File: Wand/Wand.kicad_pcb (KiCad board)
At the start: 4 copper layers, 50 x 7 mm, 20 parts, among them P1 ISP, P2 KLB4, P3 BASE, U1 ATMEGA328-MMH, U2 MAX31855KASA+, U3 MPU-6050

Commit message: Tidy up of the silk screen
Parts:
- moved C5 0.10 mm to (116.6, 112.7)

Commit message: Added back silk screen info
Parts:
- added G***: LOGO, Wand:RLAB_LOGO, B.Cu at (107.7, 112.0)
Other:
- board text added: "Hotstick - Wand"
- board text added: "Reading Hackspace - http://rlab.org.uk/"
- board text added: "rev 1 - 24/01/2016"

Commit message: Some more tidy ups
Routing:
- net /SCK: track 48.8 -> 47.4 mm
- net Net-(D1-Pad2): track 3.68 -> 4.59 mm

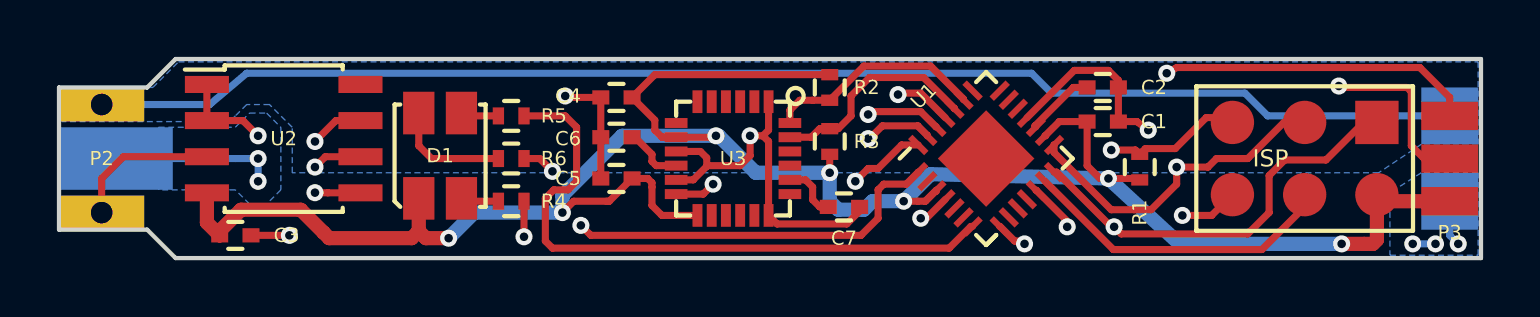
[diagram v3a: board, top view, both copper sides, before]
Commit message: Final (hopefully) tweaks to the silk screens
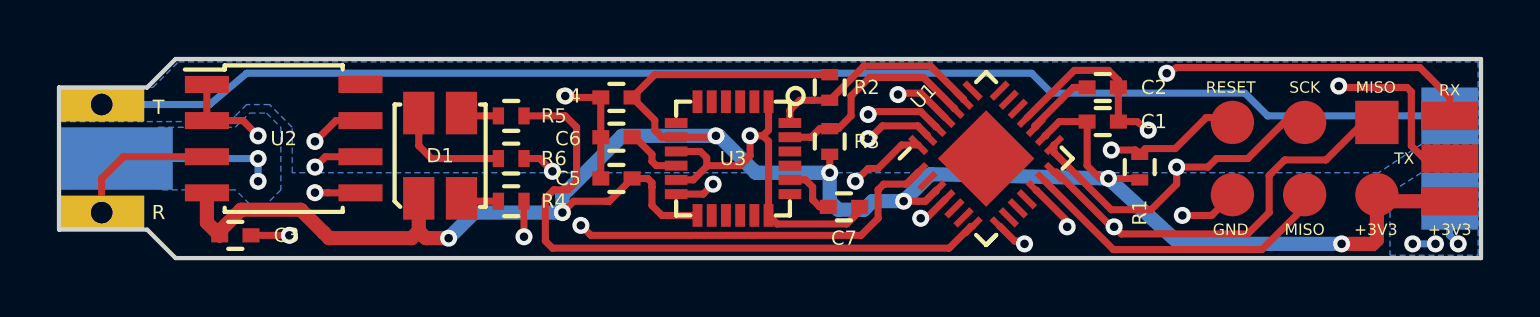
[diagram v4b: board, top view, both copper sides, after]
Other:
- board text added: "+3V3"
- board text added: "GND"
- board text added: "HEAT"
- board text added: "MISO"
- board text added: "R"
- board text added: "RESET"
- board text added: "RX"
- board text added: "SCK"
- board text added: "T"
- board text added: "TX"
- board text added: "rev 1 - 26/01/2016"
- board text removed: "rev 1 - 24/01/2016"
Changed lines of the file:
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@@
     (area 96.924999 108.424999 147.075001 115.575001)
     (thickness 1.6)
-    (drawings 17)
+    (drawings 33)
     (tracks 380)
     (zones 0)
@@
     (1 In1.Ground.Cu power hide)
     (2 In2.Signal.Cu signal hide)
-    (31 B.Power.Cu mixed)
+    (31 B.Power.Cu mixed hide)
     (32 B.Adhes user hide)
     (33 F.Adhes user hide)
     (34 B.Paste user)
     (35 F.Paste user hide)
-    (36 B.SilkS user hide)
-    (37 F.SilkS user hide)
+    (36 B.SilkS user)
+    (37 F.SilkS user)
     (38 B.Mask user)
     (39 F.Mask user)
@@
   (module Wand:Base_Connector (layer F.Signal.Cu)
     (at 145.9 112)
-    (fp_text reference P3 (at 0 2.6) (layer F.SilkS)
+    (fp_text reference P3 (at 0 2.6) (layer F.Fab)
       (effects (font (size 0.5 0.5) (thickness 0.125)))
     )
@@
   (module Wand:Jack_3.5mm_KLB (layer B.Power.Cu)
     (at 98.5 112)
-    (fp_text reference P2 (at 0 0) (layer F.SilkS)
+    (fp_text reference P2 (at 0 0) (layer F.Fab)
       (effects (font (size 0.5 0.5) (thickness 0.125)))
     )
@@
       (net 14 /SENS))
     (pad S smd rect (at 0.5 0) (size 4 2.2) (layers B.Power.Cu B.Paste B.Mask)
-      (net 2 GND))
-  )
-  (module Wand:ISP_pads_2x3 (layer F.Signal.Cu)
-    (at 140.8 112 270)
-    (fp_text reference P1 (at -3.1 0 360) (layer F.Fab)
-      (effects (font (size 0.5 0.5) (thickness 0.125)))
-    )
-    (fp_text value ISP (at 0 1.2 360) (layer F.SilkS)
-      (effects (font (size 0.6 0.6) (thickness 0.15)))
-    )
-    (fp_line (start -2.54 -3.81) (end 2.54 -3.81) (layer F.SilkS) (width 0.15))
-    (fp_line (start 2.54 -3.81) (end 2.54 3.81) (layer F.SilkS) (width 0.15))
-    (fp_line (start 2.54 3.81) (end -2.54 3.81) (layer F.SilkS) (width 0.15))
-    (fp_line (start -2.54 3.81) (end -2.54 -3.81) (layer F.SilkS) (width 0.15))
-    (pad 1 connect rect (at -1.27 -2.54 270) (size 1.524 1.524) (layers F.Signal.Cu F.Mask)
-      (net 9 /MISO))
-    (pad 2 connect circle (at 1.27 -2.54 270) (size 1.524 1.524) (layers F.Signal.Cu F.Mask)
-      (net 1 +3V3))
-    (pad 3 connect circle (at -1.27 0 270) (size 1.524 1.524) (layers F.Signal.Cu F.Mask)
-      (net 10 /SCK))
-    (pad 4 connect circle (at 1.27 0 270) (size 1.524 1.524) (layers F.Signal.Cu F.Mask)
-      (net 11 /MOSI))
-    (pad 5 connect circle (at -1.27 2.54 270) (size 1.524 1.524) (layers F.Signal.Cu F.Mask)
-      (net 12 /RESET))
-    (pad 6 connect circle (at 1.27 2.54 270) (size 1.524 1.524) (layers F.Signal.Cu F.Mask)
       (net 2 GND))
   )
@@
       (xy 0.587375 0.460375) (xy 0.79375 0.460375) (xy 0.79375 0.238125)) (layer B.SilkS) (width 0.01))
   )
-  (gr_text "rev 1 - 24/01/2016" (at 139.5 113.1) (layer B.SilkS)
+  (module Wand:ISP_pads_2x3 (layer F.Signal.Cu)
+    (at 140.8 112 270)
+    (fp_text reference P1 (at -3.1 0 360) (layer F.Fab)
+      (effects (font (size 0.5 0.5) (thickness 0.125)))
+    )
+    (fp_text value ISP (at 0 1.2 360) (layer F.Fab)
+      (effects (font (size 0.6 0.6) (thickness 0.15)))
+    )
+    (pad 1 connect rect (at -1.27 -2.54 270) (size 1.524 1.524) (layers F.Signal.Cu F.Mask)
+      (net 9 /MISO))
+    (pad 2 connect circle (at 1.27 -2.54 270) (size 1.524 1.524) (layers F.Signal.Cu F.Mask)
+      (net 1 +3V3))
+    (pad 3 connect circle (at -1.27 0 270) (size 1.524 1.524) (layers F.Signal.Cu F.Mask)
+      (net 10 /SCK))
+    (pad 4 connect circle (at 1.27 0 270) (size 1.524 1.524) (layers F.Signal.Cu F.Mask)
+      (net 11 /MOSI))
+    (pad 5 connect circle (at -1.27 2.54 270) (size 1.524 1.524) (layers F.Signal.Cu F.Mask)
+      (net 12 /RESET))
+    (pad 6 connect circle (at 1.27 2.54 270) (size 1.524 1.524) (layers F.Signal.Cu F.Mask)
+      (net 2 GND))
+  )
+  (gr_text R (at 100.5 113.9) (layer B.SilkS)
     (effects (font (size 0.5 0.5) (thickness 0.125)) (justify mirror))
   )
+  (gr_text T (at 100.5 110.2) (layer B.SilkS)
+    (effects (font (size 0.5 0.5) (thickness 0.125)) (justify mirror))
+  )
+  (gr_text GND (at 101.6 112 270) (layer B.SilkS)
+    (effects (font (size 0.4 0.4) (thickness 0.1)) (justify mirror))
+  )
+  (gr_text GND (at 145.9 112) (layer B.SilkS)
+    (effects (font (size 0.4 0.4) (thickness 0.1)) (justify mirror))
+  )
+  (gr_text HEAT (at 145.9 109) (layer B.SilkS)
+    (effects (font (size 0.4 0.4) (thickness 0.1)) (justify mirror))
+  )
+  (gr_text GND (at 138.2 114.5) (layer F.SilkS)
+    (effects (font (size 0.4 0.4) (thickness 0.1)))
+  )
+  (gr_text +3V3 (at 143.3 114.5) (layer F.SilkS)
+    (effects (font (size 0.4 0.4) (thickness 0.1)))
+  )
+  (gr_text MISO (at 140.8 114.5) (layer F.SilkS)
+    (effects (font (size 0.4 0.4) (thickness 0.1)))
+  )
+  (gr_text MISO (at 143.3 109.5) (layer F.SilkS)
+    (effects (font (size 0.4 0.4) (thickness 0.1)))
+  )
+  (gr_text SCK (at 140.8 109.5) (layer F.SilkS)
+    (effects (font (size 0.4 0.4) (thickness 0.1)))
+  )
+  (gr_text RESET (at 138.2 109.5) (layer F.SilkS)
+    (effects (font (size 0.4 0.4) (thickness 0.1)))
+  )
+  (gr_text TX (at 144.3 112) (layer F.SilkS)
+    (effects (font (size 0.4 0.4) (thickness 0.1)))
+  )
+  (gr_text +3V3 (at 145.9 114.5) (layer F.SilkS)
+    (effects (font (size 0.4 0.4) (thickness 0.1)))
+  )
+  (gr_text RX (at 145.9 109.6) (layer F.SilkS)
+    (effects (font (size 0.4 0.4) (thickness 0.1)))
+  )
+  (gr_text R (at 100.5 113.9) (layer F.SilkS)
+    (effects (font (size 0.5 0.5) (thickness 0.125)))
+  )
+  (gr_text T (at 100.5 110.2) (layer F.SilkS)
+    (effects (font (size 0.5 0.5) (thickness 0.125)))
+  )
+  (gr_text "rev 1 - 26/01/2016" (at 139.5 113.1) (layer B.SilkS)
+    (effects (font (size 0.5 0.5) (thickness 0.125)) (justify mirror))
+  )

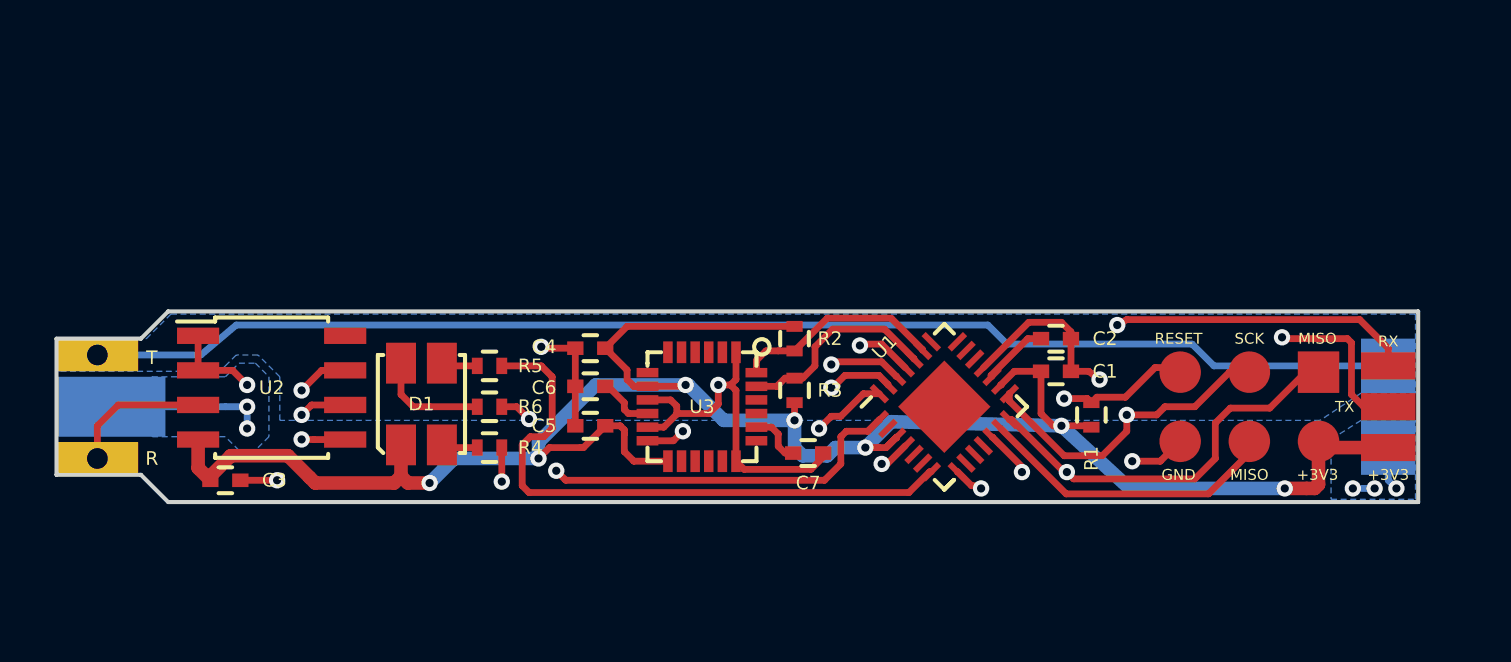
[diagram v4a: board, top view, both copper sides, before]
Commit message: Removed the capacitor from the Temp sensor to allow it to be centred and initial modifications to allow monitoring of when the tip is being heated.
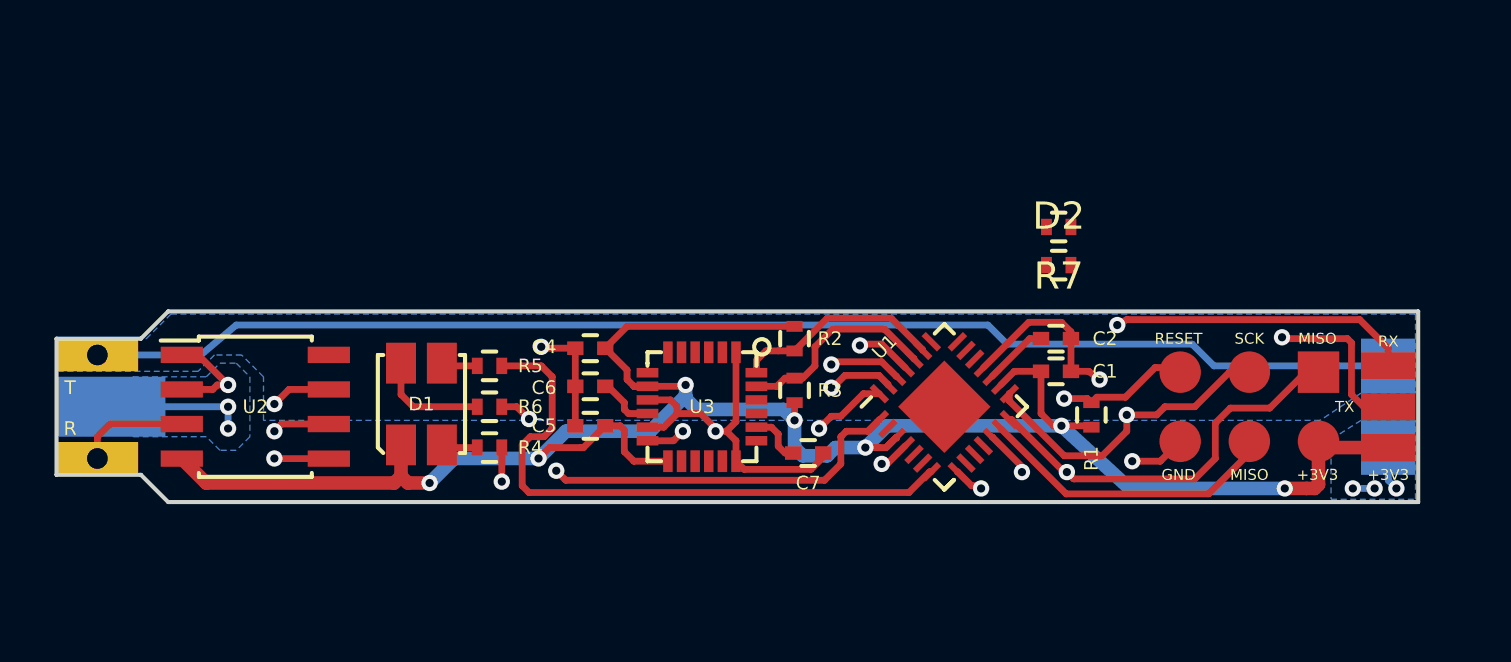
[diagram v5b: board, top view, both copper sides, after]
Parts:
- removed C3: 100n, Capacitors_SMD:C_0402
- removed G***: LOGO, Wand:RLAB_LOGO
- added D2: 3V3, Resistors_SMD:R_0402, F.Cu at (133.8, 106.8)
- added R7: 10K, Resistors_SMD:R_0402, F.Cu at (133.8, 105.4)
- moved U2 0.92 mm to (104.3, 112.0)
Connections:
- U1 pad 19: Net-(U1-Pad19) -> /HEAT_DETECT
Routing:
- net GND: track 93.7 -> 90.4 mm, vias 12 -> 11
- net /SCK: track 47.4 -> 49.1 mm
- net /TIP_TEMP_SELECT: track 32.8 -> 34.4 mm
- net /MISO: track 47.4 -> 49.0 mm
- net +3V3: track 80.5 -> 79.0 mm
- net /MPU_INT: track 9.45 -> 10.9 mm
- net /SENS: track 5.22 -> 4.09 mm

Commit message: Removed reset pull-up (should not be needed as internally pulled up) to make room for the heat detect logic and layed out the remaining components for the heat detect.
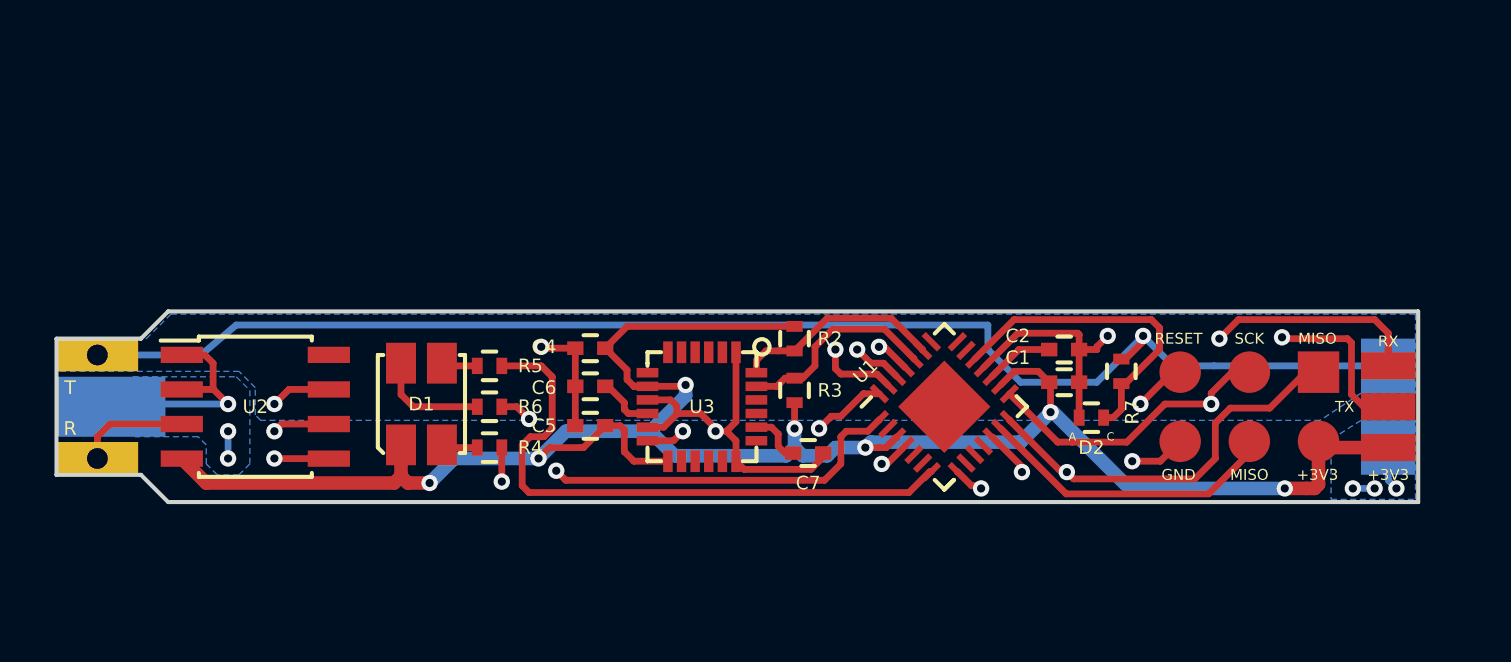
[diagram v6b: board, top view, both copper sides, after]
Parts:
- removed R1: 10K, Resistors_SMD:R_0402
- moved R7 5.78 mm to (136.1, 110.7), turned to 270 degrees
- moved D2 5.73 mm to (135.0, 112.4), turned to 180 degrees
- moved C2 0.50 mm to (134.0, 109.9)
- moved C1 0.50 mm to (134.0, 111.1)
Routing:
- net /HEAT_DETECT: track 0.00 -> 12.0 mm
- net GND: track 90.4 -> 94.7 mm
- net /SCK: track 49.1 -> 52.4 mm
- net /HEAT: track 48.4 -> 51.6 mm, vias 0 -> 1
- net /TX: track 25.8 -> 27.1 mm
- net /RESET: track 20.4 -> 21.0 mm
- net /RX: track 24.9 -> 24.3 mm
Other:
- board text added: "A"
- board text added: "C"
